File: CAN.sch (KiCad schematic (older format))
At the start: 6 parts, among them U9 TLE7250VSJ

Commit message: Replaced the 10k-Resistor with one that is in stock
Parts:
- R22: Buy https://www.digikey.com/product-detail/en/yageo/RC0603FR-07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 -> https://www.digikey.com/product-detail/en/bourns-inc/CR0603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
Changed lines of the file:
@@
 F 2 "Resistor_SMD:R_0603_1608Metric" V 880 2200 50  0001 C CNN
 F 3 "" H 950 2200 50  0001 C CNN
-F 4 "https://www.digikey.com/product-detail/en/yageo/RC0603FR-0710KL/311-10.0KHRCT-ND/729827" V 950 2200 50  0001 C CNN "Buy"
+F 4 "https://www.digikey.com/product-detail/en/bourns-inc/CR0603-FX-1002HLF/CR0603-FX-1002HLFCT-ND/3925297" V 950 2200 50  0001 C CNN "Buy"
 	1    950  2200
 	0    1    1    0

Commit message: Replaced the 100nF Low-Voltage-Caps with one, which is still in stock
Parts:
- C32, C33: Buy https://www.digikey.com/product-detail/en/kemet/C0603C104K3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 -> https://www.digikey.com/product-detail/en/murata-electronic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
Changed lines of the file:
@@
 F 2 "Capacitor_SMD:C_0603_1608Metric" H 1900 1500 50  0001 C CNN
 F 3 "" H 1900 1500 50  0001 C CNN
-F 4 "https://www.digikey.com/product-detail/en/kemet/C0603C104K3RACTU/399-1281-1-ND/416057" V 1900 1500 50  0001 C CNN "Buy"
+F 4 "https://www.digikey.com/product-detail/en/murata-electronics-north-america/GCM188R71C104KA37D/490-4774-1-ND/1641693" V 1900 1500 50  0001 C CNN "Buy"
 	1    1900 1500
 	0    1    1    0
@@
 F 2 "Capacitor_SMD:C_0603_1608Metric" H 1500 1500 50  0001 C CNN
 F 3 "" H 1500 1500 50  0001 C CNN
-F 4 "https://www.digikey.com/product-detail/en/kemet/C0603C104K3RACTU/399-1281-1-ND/416057" V 1500 1500 50  0001 C CNN "Buy"
+F 4 "https://www.digikey.com/product-detail/en/murata-electronics-north-america/GCM188R71C104KA37D/490-4774-1-ND/1641693" V 1500 1500 50  0001 C CNN "Buy"
 	1    1500 1500
 	0    1    1    0

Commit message: Removed the LV-Caps with the HV-Caps to remain consistent
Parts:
- C32, C33: footprint Capacitor_SMD:C_0603_1608Metric -> Capacitor_SMD:C_0805_2012Metric; Buy https://www.digikey.com/product-detail/en/murata-electronics-north-america/GCM188R71C104KA37D/490-4774-1-ND/1641693 -> https://www.digikey.com/product-detail/en/murata-electronics-north-america/GCM21BR72A104KA37L/490-4789-1-ND/1641708
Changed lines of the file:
@@
 F 0 "C33" V 2000 1450 50  0000 L CNN
 F 1 "100nF" V 1800 1400 50  0000 L CNN
-F 2 "Capacitor_SMD:C_0603_1608Metric" H 1900 1500 50  0001 C CNN
+F 2 "Capacitor_SMD:C_0805_2012Metric" H 1900 1500 50  0001 C CNN
 F 3 "" H 1900 1500 50  0001 C CNN
-F 4 "https://www.digikey.com/product-detail/en/murata-electronics-north-america/GCM188R71C104KA37D/490-4774-1-ND/1641693" V 1900 1500 50  0001 C CNN "Buy"
+F 4 "https://www.digikey.com/product-detail/en/murata-electronics-north-america/GCM21BR72A104KA37L/490-4789-1-ND/1641708" V 1900 1500 50  0001 C CNN "Buy"
 	1    1900 1500
 	0    1    1    0
@@
 F 0 "C32" V 1600 1450 50  0000 L CNN
 F 1 "100nF" V 1400 1400 50  0000 L CNN
-F 2 "Capacitor_SMD:C_0603_1608Metric" H 1500 1500 50  0001 C CNN
+F 2 "Capacitor_SMD:C_0805_2012Metric" H 1500 1500 50  0001 C CNN
 F 3 "" H 1500 1500 50  0001 C CNN
-F 4 "https://www.digikey.com/product-detail/en/murata-electronics-north-america/GCM188R71C104KA37D/490-4774-1-ND/1641693" V 1500 1500 50  0001 C CNN "Buy"
+F 4 "https://www.digikey.com/product-detail/en/murata-electronics-north-america/GCM21BR72A104KA37L/490-4789-1-ND/1641708" V 1500 1500 50  0001 C CNN "Buy"
 	1    1500 1500
 	0    1    1    0

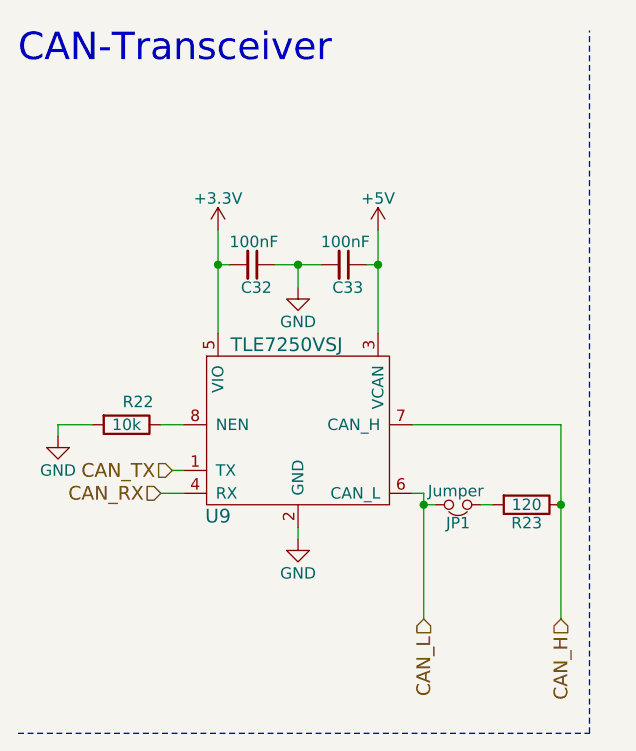
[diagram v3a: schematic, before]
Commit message: Filled in the Parts for the Fault-Indicator
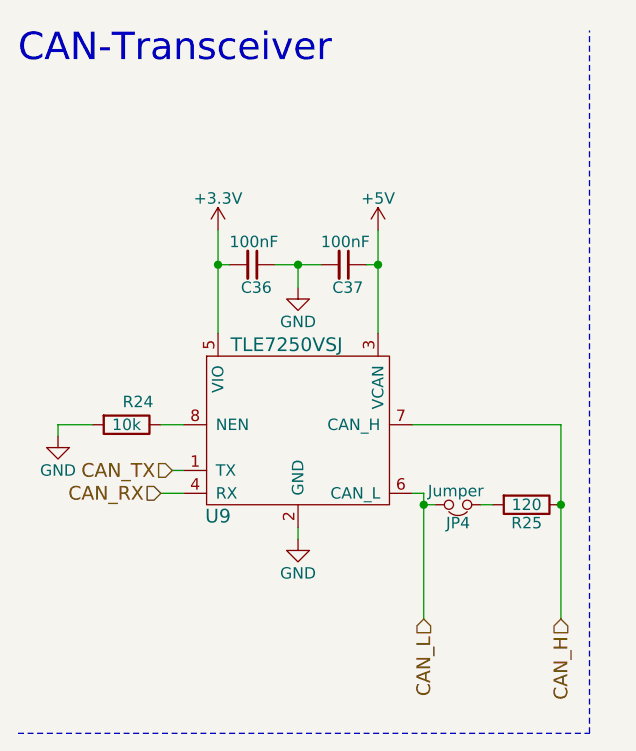
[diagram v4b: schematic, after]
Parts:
- renumbered C32 to C36, C33 to C37, JP1 to JP4, R22 to R24, R23 to R25
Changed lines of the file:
@@
 $EndDescr
 $Comp
-L power:+5V #PWR084
+L power:+5V #PWR090
 U 1 1 5A8476B7
 P 2050 1350
-F 0 "#PWR084" H 2050 1200 50  0001 C CNN
+F 0 "#PWR090" H 2050 1200 50  0001 C CNN
 F 1 "+5V" H 2050 1490 50  0000 C CNN
 F 2 "" H 2050 1350 50  0001 C CNN
@@
 $EndComp
 $Comp
-L power:+3.3V #PWR081
+L power:+3.3V #PWR087
 U 1 1 5A8476BD
 P 1350 1350
-F 0 "#PWR081" H 1350 1200 50  0001 C CNN
+F 0 "#PWR087" H 1350 1200 50  0001 C CNN
 F 1 "+3.3V" H 1350 1490 50  0000 C CNN
 F 2 "" H 1350 1350 50  0001 C CNN
@@
 $EndComp
 $Comp
-L Device:C_Small C33
+L Device:C_Small C37
 U 1 1 5A8476C5
 P 1900 1500
-F 0 "C33" V 2000 1450 50  0000 L CNN
+F 0 "C37" V 2000 1450 50  0000 L CNN
 F 1 "100nF" V 1800 1400 50  0000 L CNN
 F 2 "Capacitor_SMD:C_0805_2012Metric" H 1900 1500 50  0001 C CNN
@@
 $EndComp
 $Comp
-L Device:C_Small C32
+L Device:C_Small C36
 U 1 1 5A8476CC
 P 1500 1500
-F 0 "C32" V 1600 1450 50  0000 L CNN
+F 0 "C36" V 1600 1450 50  0000 L CNN
 F 1 "100nF" V 1400 1400 50  0000 L CNN
 F 2 "Capacitor_SMD:C_0805_2012Metric" H 1500 1500 50  0001 C CNN
@@
 $EndComp
 $Comp
-L Device:R R22
+L Device:R R24
 U 1 1 5A8476D3
 P 950 2200
-F 0 "R22" V 850 2250 50  0000 C CNN
+F 0 "R24" V 850 2250 50  0000 C CNN
 F 1 "10k" V 950 2200 50  0000 C CNN
 F 2 "Resistor_SMD:R_0603_1608Metric" V 880 2200 50  0001 C CNN
@@
 CAN-Transceiver
 $Comp
-L power:GND #PWR083
+L power:GND #PWR089
 U 1 1 5A8476DB
 P 1700 2700
-F 0 "#PWR083" H 1700 2450 50  0001 C CNN
+F 0 "#PWR089" H 1700 2450 50  0001 C CNN
 F 1 "GND" H 1700 2550 50  0000 C CNN
 F 2 "" H 1700 2700 50  0001 C CNN
@@
 $EndComp
 $Comp
-L power:GND #PWR082
+L power:GND #PWR088
 U 1 1 5A8476E1
 P 1700 1600
-F 0 "#PWR082" H 1700 1350 50  0001 C CNN
+F 0 "#PWR088" H 1700 1350 50  0001 C CNN
 F 1 "GND" H 1700 1450 50  0000 C CNN
 F 2 "" H 1700 1600 50  0001 C CNN
@@
 $EndComp
 $Comp
-L power:GND #PWR080
+L power:GND #PWR086
 U 1 1 5A8476E7
 P 650 2250
-F 0 "#PWR080" H 650 2000 50  0001 C CNN
+F 0 "#PWR086" H 650 2000 50  0001 C CNN
 F 1 "GND" H 650 2100 50  0000 C CNN
 F 2 "" H 650 2250 50  0001 C CNN
@@
 $EndComp
 $Comp
-L Device:R R23
+L Device:R R25
 U 1 1 5A8476F4
 P 2700 2550
-F 0 "R23" V 2780 2550 50  0000 C CNN
+F 0 "R25" V 2780 2550 50  0000 C CNN
 F 1 "120" V 2700 2550 50  0000 C CNN
 F 2 "Resistor_SMD:R_1206_3216Metric" V 2630 2550 50  0001 C CNN
@@
 $EndComp
 $Comp
-L Device:Jumper_NC_Small JP1
+L Device:Jumper_NC_Small JP4
 U 1 1 5A84773B
 P 2400 2550
-F 0 "JP1" H 2400 2630 50  0000 C CNN
+F 0 "JP4" H 2400 2630 50  0000 C CNN
 F 1 "Jumper" H 2410 2490 50  0000 C CNN
 F 2 "Connector_PinHeader_2.54mm:PinHeader_2x01_P2.54mm_Vertical" H 2400 2550 50  0001 C CNN

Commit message: Replaced OOS 10k-Resistor
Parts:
- R24: Buy https://www.digikey.com/product-detail/en/bourns-inc/CR0603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 -> https://www.digikey.com/short/jw22d4
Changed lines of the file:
@@
 F 2 "Resistor_SMD:R_0603_1608Metric" V 880 2200 50  0001 C CNN
 F 3 "" H 950 2200 50  0001 C CNN
-F 4 "https://www.digikey.com/product-detail/en/bourns-inc/CR0603-FX-1002HLF/CR0603-FX-1002HLFCT-ND/3925297" V 950 2200 50  0001 C CNN "Buy"
+F 4 "https://www.digikey.com/short/jw22d4" V 950 2200 50  0001 C CNN "Buy"
 	1    950  2200
 	0    1    1    0

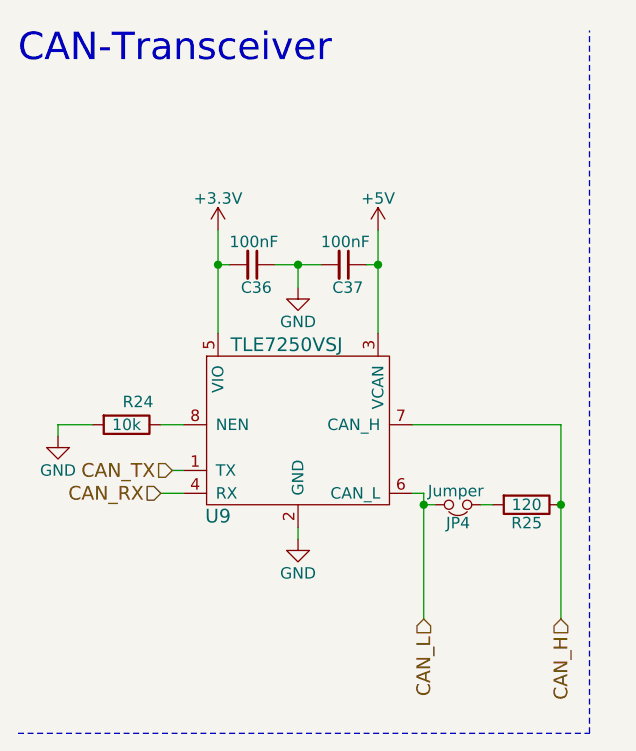
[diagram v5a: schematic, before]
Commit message: Added TestPoints the CAN-Schematic
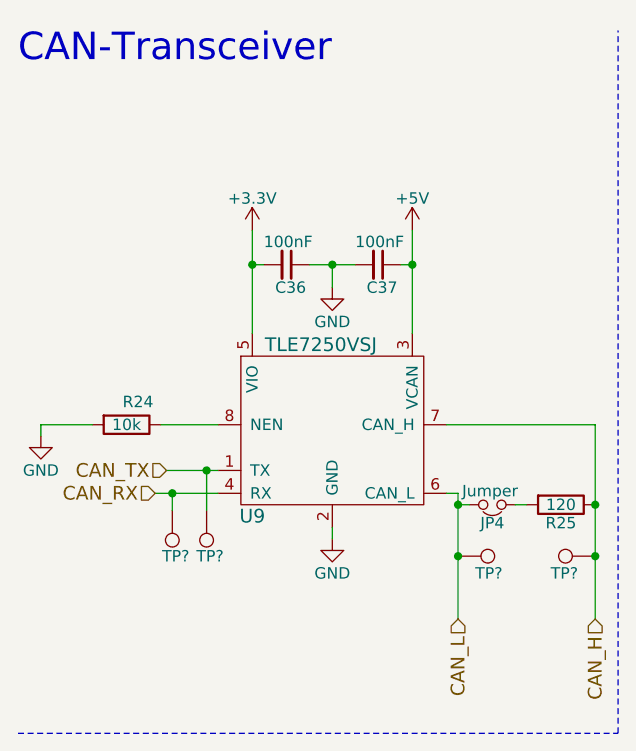
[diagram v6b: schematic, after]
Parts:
- added TP? (x4): TestPoint, symbol Connector:TestPoint
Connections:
- net CAN_H: now also TP?.1
- net CAN_L: now also TP?.1
- net CAN_RX: now also TP?.1
- net CAN_TX: now also TP?.1
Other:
- moved on the sheet: C36, C37, JP4, R25, U9
